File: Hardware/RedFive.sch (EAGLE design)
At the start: 89 parts, among them IC3 LM1117, J1 FEMALE 2x3, J2 USB Female Type C Connector, J3 POWER_JACKSUPER_BOMB_DIGITY, J4 QWIIC_RIGHT_ANGLE, J5 CORTEX_JTAG_DEBUG_PTH_NS, Q1 1.1A/60V/600mΩ, U2 1.8V, U3 AP2112-3.3V, U4 FE310, U5 32MBit, Y1 32.768KHZ, Y2 16MHz

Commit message: post review changes-v10
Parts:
- removed J1: FEMALE 2x3, SparkFun-Connectors:CONN_03X2POGO_PINS
- added I2C: JUMPER-SMT_3_NO_NO-SILK, SparkFun-Jumpers:JUMPER-SMT_3_NO_NO-SILK
- added TP1, TP2, TP3, TP4, TP5, TP6: TEST-POINT3X5, SparkFun-Connectors:TEST-POINT3X5
- D5: value YELLOW -> GREEN; device SparkFun-LED:LED-YELLOW_HIDDENSILK -> SparkFun-LED:LED-GREEN1206
- J4: value QWIIC_RIGHT_ANGLE -> QWIIC
- LED1: value Blue -> BLUE; device SparkFun-LED:LED-BLUE_HIDDENSILK -> SparkFun-LED:LED-BLUE1206
- LED3: value GREEN -> Yellow; device SparkFun-LED:LED-GREENLILYPAD -> SparkFun-LED:LED-YELLOWLILYPAD
- renumbered U$44 to U6
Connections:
- new net N$4: I2C.3, R10.2
- new net N$5: I2C.1, R9.2
- net 3.3V: now also I2C.2, TP1.1; no longer J1.2, R10.2, R9.2
- net DBG_RESET: now also TP2.1; no longer J1.4
- net DBG_SWDCLK: now also TP5.1; no longer J1.3
- net DBG_SWDIO: now also TP4.1; no longer J1.1
- net DBG_SWO: now also TP6.1; no longer J1.5
- net GND: now also TP3.1; no longer J1.6
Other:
- note added: "v10"
- note removed: "v02"
- moved on the sheet: J4, R10, R9

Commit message: post checklist changes
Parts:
- U2: value 1.8V -> AP2127K-1.8V
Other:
- note added: "Close this jumper if your I2C slave does not have it's own pullup resistors"
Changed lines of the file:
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@@
 <part name="JP15" library="SparkFun" deviceset="FIDUCIAL" device="1X2"/>
 <part name="JP16" library="SparkFun" deviceset="FIDUCIAL" device="1X2"/>
-<part name="U2" library="SparkFun-IC-Power" deviceset="V_REG_AP2127" device="K-1.8V" value="1.8V"/>
+<part name="U2" library="SparkFun-IC-Power" deviceset="V_REG_AP2127" device="K-1.8V" value="AP2127K-1.8V"/>
 <part name="GND16" library="SparkFun-PowerSymbols" deviceset="GND" device=""/>
 <part name="C9" library="SparkFun-Capacitors" deviceset="1.0UF" device="-0603-16V-10%" value="1.0uF"/>
@@
 <wire x1="248.92" y1="147.32" x2="137.16" y2="147.32" width="0.1524" layer="97" style="longdash"/>
 <text x="139.954" y="143.002" size="2.54" layer="94" font="vector">USB -&gt; JTAG</text>
+<text x="86.36" y="78.74" size="1.27" layer="94" font="vector">Close this jumper
+if your I2C slave
+does not have it's
+own pullup
+resistors</text>
 </plain>
 <instances>

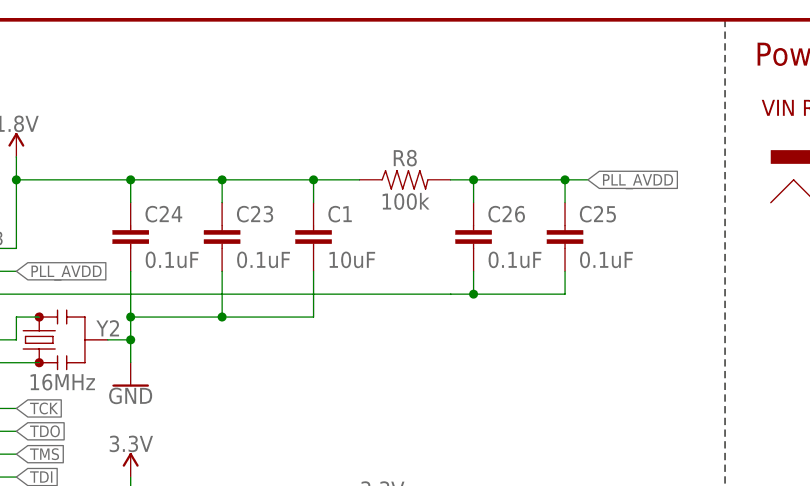
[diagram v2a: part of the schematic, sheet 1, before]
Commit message: updating R8 to 100 Ohm
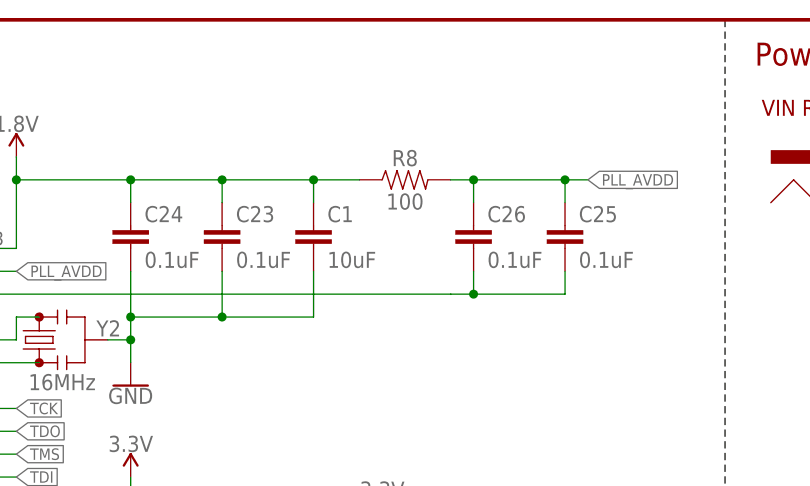
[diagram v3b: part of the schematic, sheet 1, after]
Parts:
- D5: device SparkFun-LED:LED-GREEN1206 -> SparkFun-LED:LED-GREENLILYPAD
- R8: value 100k -> 100; device SparkFun-Resistors:100KOHM-0603-1/10W-1% -> SparkFun-Resistors:100OHM-0603-1/10W-1%
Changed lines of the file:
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@@
 <part name="C25" library="SparkFun-Capacitors" deviceset="0.1UF" device="-0603-25V-(+80/-20%)" value="0.1uF"/>
 <part name="C26" library="SparkFun-Capacitors" deviceset="0.1UF" device="-0603-25V-(+80/-20%)" value="0.1uF"/>
-<part name="R8" library="SparkFun-Resistors" deviceset="100KOHM" device="-0603-1/10W-1%" value="100k"/>
+<part name="R8" library="SparkFun-Resistors" deviceset="100OHM" device="-0603-1/10W-1%" value="100"/>
 <part name="R9" library="SparkFun-Resistors" deviceset="4.7KOHM" device="-0603-1/10W-1%" value="4.7k"/>
 <part name="R10" library="SparkFun-Resistors" deviceset="4.7KOHM" device="-0603-1/10W-1%" value="4.7k"/>
@@
 <part name="SUPPLY19" library="SparkFun-PowerSymbols" deviceset="3.3V" device=""/>
 <part name="SUPPLY20" library="SparkFun-PowerSymbols" deviceset="3.3V" device=""/>
-<part name="D5" library="SparkFun-LED" deviceset="LED-GREEN" device="1206" value="GREEN"/>
+<part name="D5" library="SparkFun-LED" deviceset="LED-GREEN" device="LILYPAD" value="GREEN"/>
 <part name="R21" library="SparkFun-Resistors" deviceset="4.7KOHM" device="-0603-1/10W-1%" value="4.7k"/>
 <part name="R22" library="SparkFun-Resistors" deviceset="4.7KOHM" device="-0603-1/10W-1%" value="4.7k"/>
